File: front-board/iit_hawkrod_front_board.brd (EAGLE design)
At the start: 65 x 100 mm, 29 parts

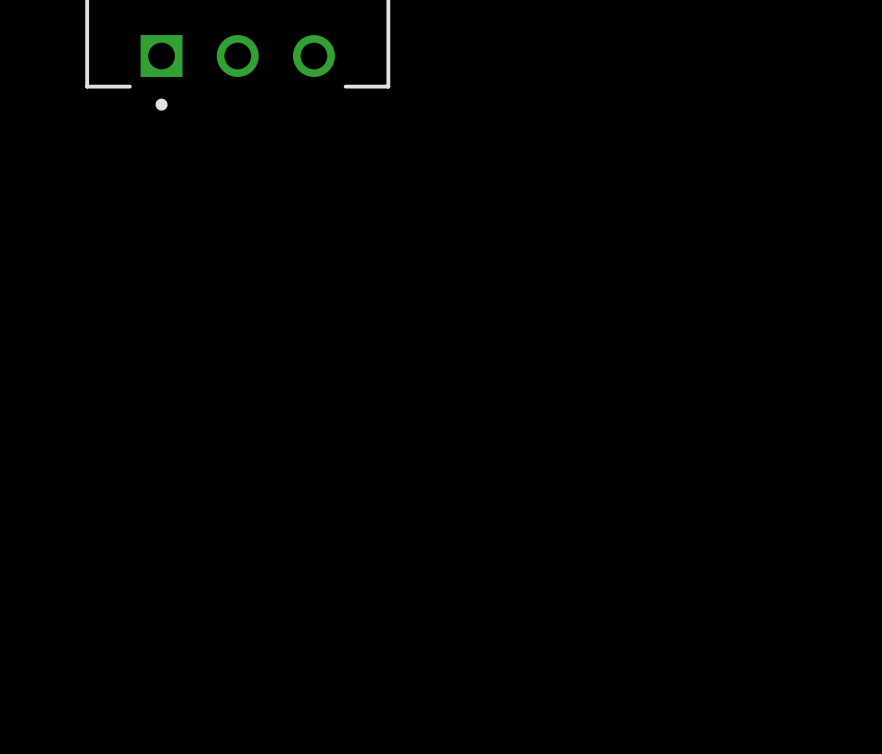
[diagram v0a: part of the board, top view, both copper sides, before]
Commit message: Add Status Lights
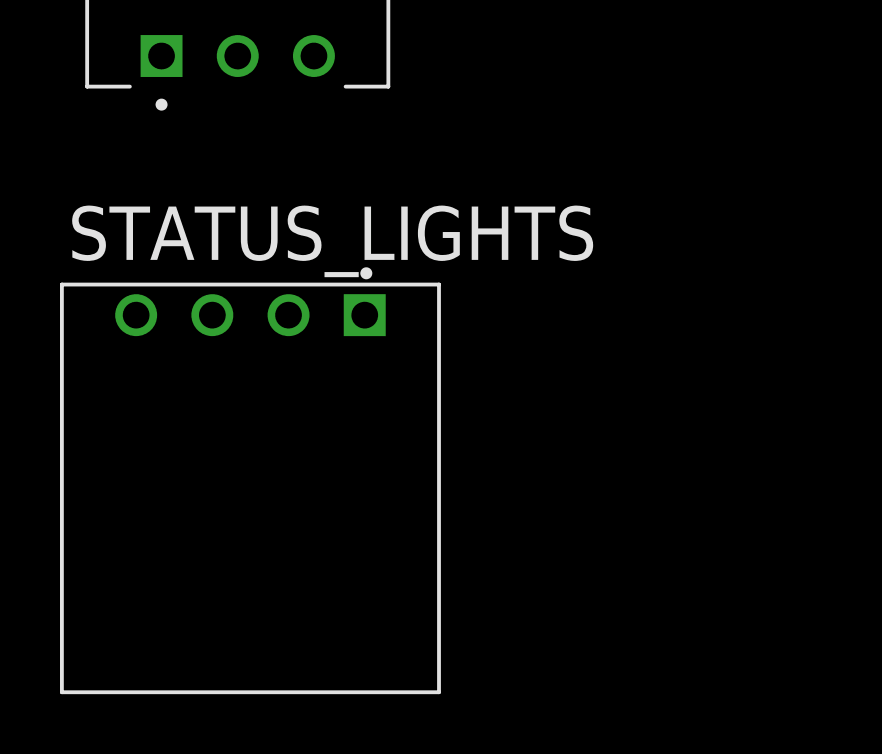
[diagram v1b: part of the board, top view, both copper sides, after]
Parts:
- added STATUS_LIGHTS: 5-103635-3, 5-103635-3:TE_5-103635-3
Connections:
- new net SIG_HRT_LED: STATUS_LIGHTS.4, U$6.13-SCK/LED
- net 5V: now also STATUS_LIGHTS.1
- net GND: now also STATUS_LIGHTS.2, STATUS_LIGHTS.3
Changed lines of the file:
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@@
 <attribute name="VALUE" x="-98.4562" y="-133.12888125" size="1.27" layer="27"/>
+</element>
+<element name="STATUS_LIGHTS" library="5-103635-3" package="TE_5-103635-3" value="5-103635-3" x="-92.26278125" y="-138.076609375" smashed="yes">
+<attribute name="AVAILABILITY" value="In Stock" x="-105.55810625" y="-118.09128125" size="1.778" layer="27" display="off"/>
+<attribute name="COMMENT" value="5-103635-3" x="-105.55810625" y="-118.09128125" size="1.778" layer="27" display="off"/>
+<attribute name="DESCRIPTION" value=" Header, Through Hole; Shrouded; Right Angle; Brass; Thermoplastic; 4; 0.1 in. " x="-105.55810625" y="-118.09128125" size="1.778" layer="27" display="off"/>
+<attribute name="EU_ROHS_COMPLIANCE" value="Compliant" x="-105.55810625" y="-118.09128125" size="1.778" layer="27" display="off"/>
+<attribute name="MF" value="TE Connectivity" x="-105.55810625" y="-118.09128125" size="1.778" layer="27" display="off"/>
+<attribute name="MP" value="5-103635-3" x="-105.55810625" y="-118.09128125" size="1.778" layer="27" display="off"/>
+<attribute name="NAME" x="-98.3509125" y="-136.23511875" size="1.77848125" layer="25"/>
+<attribute name="PACKAGE" value="None" x="-105.55810625" y="-118.09128125" size="1.778" layer="27" display="off"/>
+<attribute name="PRICE" value="None" x="-105.55810625" y="-118.09128125" size="1.778" layer="27" display="off"/>
+<attribute name="PURCHASE-URL" value="https://pricing.snapeda.com/search/part/5-103635-3/?ref=eda" x="-105.55810625" y="-118.09128125" size="1.778" layer="27" display="off"/>
+<attribute name="VALUE" x="-98.363521875" y="-153.022909375" size="1.778509375" layer="27"/>
 </element>
 </elements>
@@
 <contactref element="L_WHEEL_SENSOR" pad="2"/>
 <contactref element="R_WHEEL_SENSOR" pad="2"/>
+<contactref element="STATUS_LIGHTS" pad="2"/>
+<contactref element="STATUS_LIGHTS" pad="3"/>
+<wire x1="-90.99278125" y1="-138.076609375" x2="-93.53278125" y2="-138.076609375" width="0" layer="19" extent="1-1"/>
+<wire x1="-92.6862" y1="-129.43888125" x2="-93.53278125" y2="-138.076609375" width="0" layer="19" extent="1-1"/>
 <wire x1="-86.27496875" y1="-110.97785625" x2="-92.6862" y2="-129.43888125" width="0" layer="19" extent="1-1"/>
 <wire x1="-86.27496875" y1="-104.79595625" x2="-86.27496875" y2="-110.97785625" width="0" layer="19" extent="1-1"/>
@@
 <contactref element="L_WHEEL_SENSOR" pad="1"/>
 <contactref element="R_WHEEL_SENSOR" pad="1"/>
+<contactref element="STATUS_LIGHTS" pad="1"/>
+<wire x1="-95.2262" y1="-129.43888125" x2="-88.45278125" y2="-138.076609375" width="0" layer="19" extent="1-1"/>
 <wire x1="-95.2262" y1="-109.7922875" x2="-95.2262" y2="-129.43888125" width="0" layer="19" extent="1-1"/>
 <wire x1="-83.581190625" y1="-72.7432125" x2="-95.2262" y2="-109.7922875" width="0" layer="19" extent="1-1"/>
@@
 <wire x1="4.576471875" y1="-9.8671625" x2="-90.1462" y2="-129.43888125" width="0" layer="19" extent="1-1"/>
 </signal>
+<signal name="SIG_HRT_LED">
+<contactref element="U$6" pad="13-SCK/LED"/>
+<contactref element="STATUS_LIGHTS" pad="4"/>
+<wire x1="24.896471875" y1="-9.8671625" x2="-96.07278125" y2="-138.076609375" width="0" layer="19" extent="1-1"/>
+</signal>
 </signals>

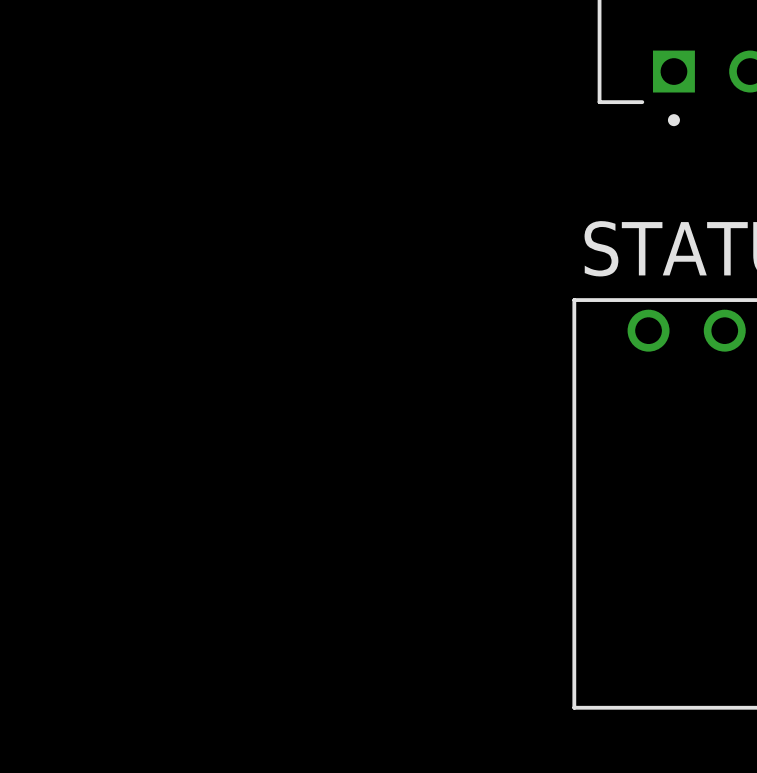
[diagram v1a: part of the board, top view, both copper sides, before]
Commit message: Add USB
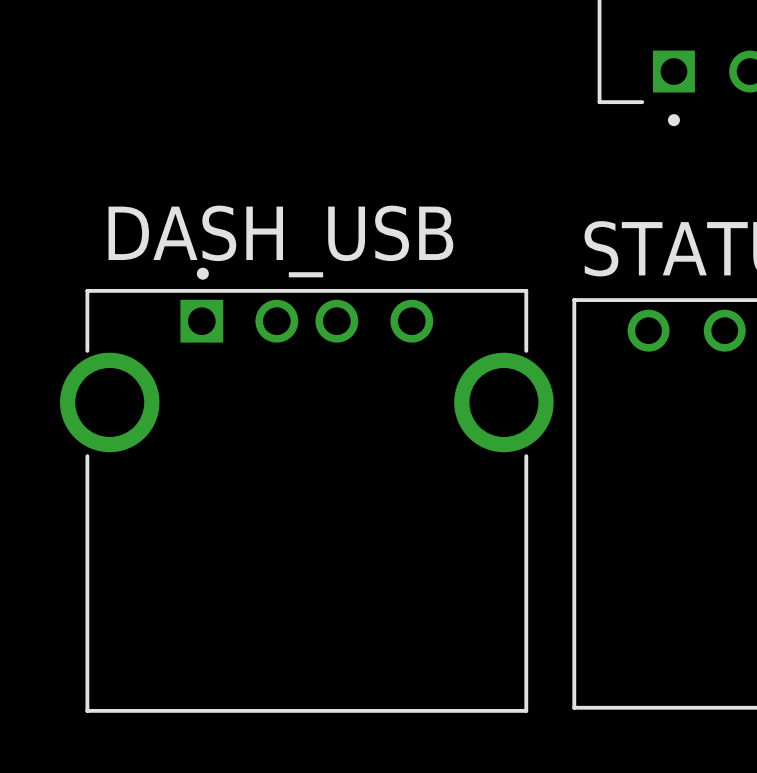
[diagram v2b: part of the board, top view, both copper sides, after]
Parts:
- added DASH_USB: 1-292303-1, 1-292303-1:TE_1-292303-1
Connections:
- new net N$13: DASH_USB.3, U$6.D-
- new net N$16: DASH_USB.2, U$6.D+
- net 5V: now also DASH_USB.4
- net GND: now also DASH_USB.1, DASH_USB.S1, DASH_USB.S2
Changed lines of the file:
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@@
 <attribute name="VALUE" x="-98.363521875" y="-153.022909375" size="1.778509375" layer="27"/>
+</element>
+<element name="DASH_USB" library="1-292303-1" package="TE_1-292303-1" value="1-292303-1" x="-107.4634875" y="-143.7504125" smashed="yes">
+<attribute name="AVAILABILITY" value="In Stock" x="-107.4634875" y="-143.7504125" size="1.778" layer="27" display="off"/>
+<attribute name="COMMENT" value="1-292303-1" x="-107.4634875" y="-143.7504125" size="1.778" layer="27" display="off"/>
+<attribute name="DESCRIPTION" value=" Conn USB 2.0 Type A RCP 4 POS Solder RA SMD 4 Terminal 1 Port Box/Tray " x="-107.4634875" y="-143.7504125" size="1.778" layer="27" display="off"/>
+<attribute name="EU_ROHS_COMPLIANCE" value="Compliant" x="-107.4634875" y="-143.7504125" size="1.778" layer="27" display="off"/>
+<attribute name="MF" value="TE Connectivity" x="-107.4634875" y="-143.7504125" size="1.778" layer="27" display="off"/>
+<attribute name="MP" value="1-292303-1" x="-107.4634875" y="-143.7504125" size="1.778" layer="27" display="off"/>
+<attribute name="NAME" x="-114.28931875" y="-135.72223125" size="1.78148125" layer="25"/>
+<attribute name="PACKAGE" value="None" x="-107.4634875" y="-143.7504125" size="1.778" layer="27" display="off"/>
+<attribute name="PRICE" value="None" x="-107.4634875" y="-143.7504125" size="1.778" layer="27" display="off"/>
+<attribute name="PURCHASE-URL" value="https://pricing.snapeda.com/search/part/1-292303-1/?ref=eda" x="-107.4634875" y="-143.7504125" size="1.778" layer="27" display="off"/>
+<attribute name="VALUE" x="-114.40125625" y="-152.988271875" size="1.77806875" layer="27"/>
 </element>
 </elements>
@@
 <contactref element="STATUS_LIGHTS" pad="2"/>
 <contactref element="STATUS_LIGHTS" pad="3"/>
+<contactref element="DASH_USB" pad="1"/>
+<contactref element="DASH_USB" pad="S1"/>
+<contactref element="DASH_USB" pad="S2"/>
+<wire x1="-110.9634875" y1="-137.7604125" x2="-114.0334875" y2="-140.4704125" width="0" layer="19" extent="1-1"/>
+<wire x1="-100.8934875" y1="-140.4704125" x2="-110.9634875" y2="-137.7604125" width="0" layer="19" extent="1-1"/>
+<wire x1="-93.53278125" y1="-138.076609375" x2="-100.8934875" y2="-140.4704125" width="0" layer="19" extent="1-1"/>
 <wire x1="-90.99278125" y1="-138.076609375" x2="-93.53278125" y2="-138.076609375" width="0" layer="19" extent="1-1"/>
 <wire x1="-92.6862" y1="-129.43888125" x2="-93.53278125" y2="-138.076609375" width="0" layer="19" extent="1-1"/>
@@
 <contactref element="R_WHEEL_SENSOR" pad="1"/>
 <contactref element="STATUS_LIGHTS" pad="1"/>
-<wire x1="-95.2262" y1="-129.43888125" x2="-88.45278125" y2="-138.076609375" width="0" layer="19" extent="1-1"/>
+<contactref element="DASH_USB" pad="4"/>
+<wire x1="-95.2262" y1="-129.43888125" x2="-103.9634875" y2="-137.7604125" width="0" layer="19" extent="1-1"/>
+<wire x1="-88.45278125" y1="-138.076609375" x2="-95.2262" y2="-129.43888125" width="0" layer="19" extent="1-1"/>
 <wire x1="-95.2262" y1="-109.7922875" x2="-95.2262" y2="-129.43888125" width="0" layer="19" extent="1-1"/>
 <wire x1="-83.581190625" y1="-72.7432125" x2="-95.2262" y2="-109.7922875" width="0" layer="19" extent="1-1"/>
@@
 <wire x1="24.896471875" y1="-9.8671625" x2="-96.07278125" y2="-138.076609375" width="0" layer="19" extent="1-1"/>
 </signal>
+<signal name="N$13">
+<contactref element="U$6" pad="D-"/>
+<contactref element="DASH_USB" pad="3"/>
+<wire x1="-7.893528125" y1="-16.4871625" x2="-106.4634875" y2="-137.7604125" width="0" layer="19" extent="1-1"/>
+</signal>
+<signal name="N$16">
+<contactref element="U$6" pad="D+"/>
+<contactref element="DASH_USB" pad="2"/>
+<wire x1="-7.893528125" y1="-18.4871625" x2="-108.4634875" y2="-137.7604125" width="0" layer="19" extent="1-1"/>
+</signal>
 </signals>

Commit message: Layout_Pre
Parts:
- moved DASH_USB 284.7 mm to (51.1, 92.7), turned to 180 degrees
- moved R_WHEEL_SENSOR 249.2 mm to (52.1, 73.3), turned to 270 degrees
- moved STATUS_LIGHTS 240.4 mm to (52.2, 54.1), turned to 90 degrees
- moved R20 200.6 mm to (10.5, 65.6)
- moved R19 199.2 mm to (10.5, 70.1)
- moved L_WHEEL_SENSOR 197.4 mm to (12.9, 57.0), flipped to the bottom, turned to 270 degrees
- moved R16 193.3 mm to (17.1, 65.6)
- moved R10 181.8 mm to (17.1, 70.5), flipped to the bottom
- moved R15 181.2 mm to (3.81, 65.6)
- moved DRIVE_CONTROLS 180.2 mm to (12.9, 84.0), turned to 90 degrees
- moved R14 179.6 mm to (3.73, 70.0)
- moved R8 164.1 mm to (60.8, 21.2)
- moved START_BUTTON 140.8 mm to (52.3, 10.8), turned to 90 degrees
- moved FAULT_INDICATORS 137.8 mm to (52.2, 32.9), turned to 90 degrees
- moved R18 109.8 mm to (4.57, 42.0)
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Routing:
- net N$4: track 13.0 -> 64.6 mm
- net 3.3V: track 48.3 -> 95.2 mm
- net N$8: track 51.4 -> 82.4 mm
- net SIG_BMS_FAULT: track 36.6 -> 62.8 mm
- net SIG_START_LED: track 41.0 -> 63.2 mm
- net SIG_IMD_FAULT: track 23.1 -> 32.4 mm
- net N$2: track 5.43 -> 14.4 mm
- net N$3: track 19.9 -> 22.7 mm
- net N$5: track 6.32 -> 3.96 mm
